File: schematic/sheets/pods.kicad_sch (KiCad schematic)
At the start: 41 parts, among them J1 WATER-1x03, J2 SOIL-1x03, J3 LIGHT-SENS-1x03, J4 PROG-1x04, M1 PUMP-5V-1A, Q1 IRLZ44N, Q2 IRLZ44N, SW1 BOOT-TACT, U1A ESP32-CAM-ODD, U1B ESP32-CAM-EVEN, U2 DHT22

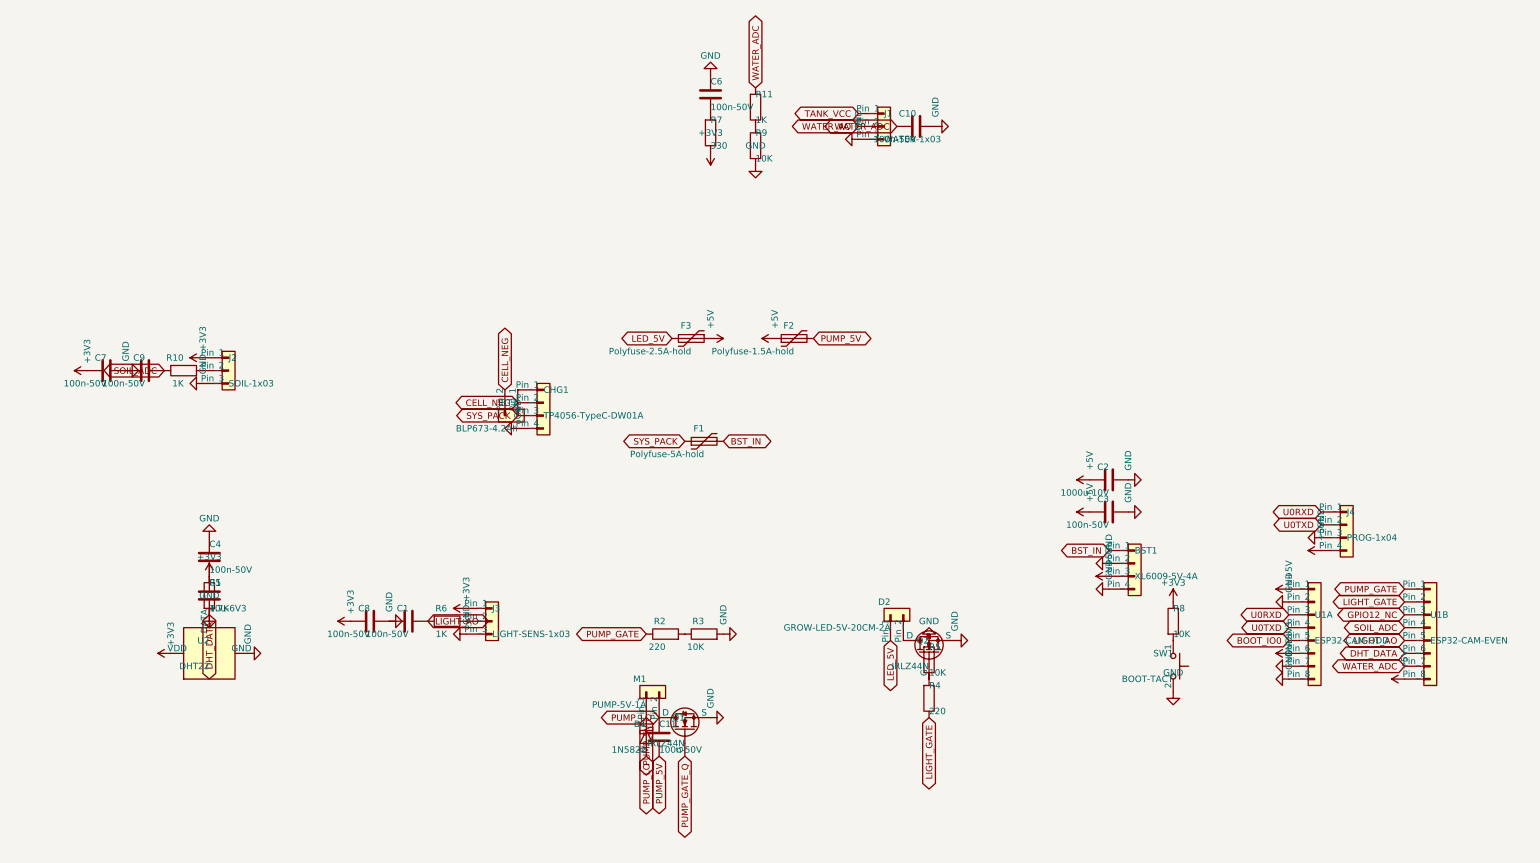
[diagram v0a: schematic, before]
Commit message: Organize schematic/: sheets/ mfg/ final/, drop sklib
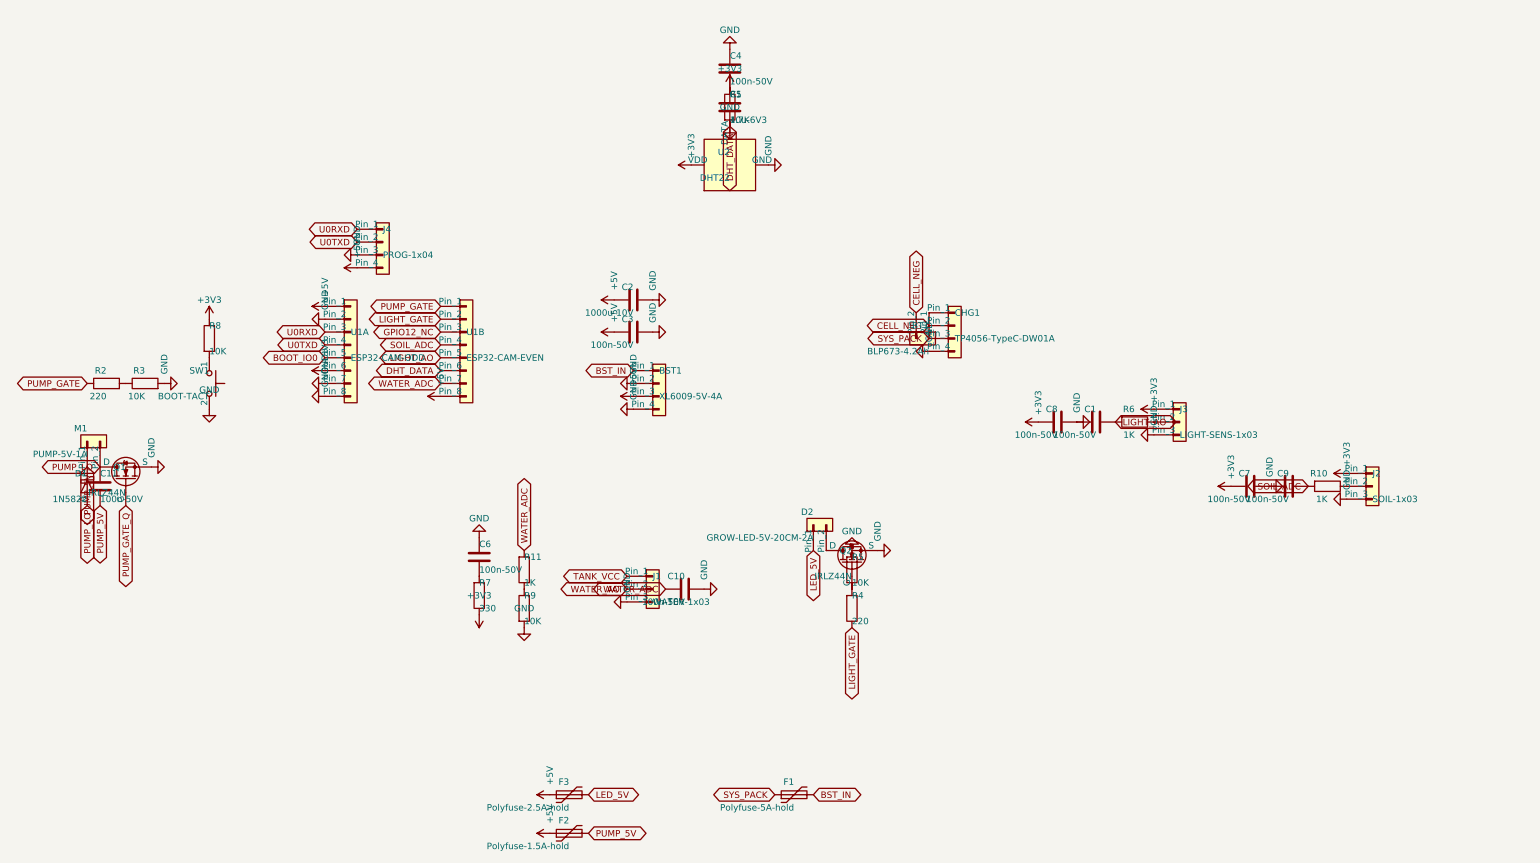
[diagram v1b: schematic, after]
